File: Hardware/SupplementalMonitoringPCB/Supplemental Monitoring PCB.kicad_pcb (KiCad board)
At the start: 2 copper layers, 41.8 x 30.1 mm, 67 parts, among them J6 52465-2470, U10 INND-SS30RAB, U11 INND-SS30RAB, U2 SN74HCS595DYYR, U4 SN74HCS595DYYR, U5 TLV9002QDRQ1, U6 TLV9002QDRQ1, U7 INND-SS30RAB, U8 SN74HCS595DYYR

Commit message: schm actually done now whoops
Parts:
- U4: moved to B.Cu
- moved U4 100.5 mm to (211.9, 65.0), turned to 180 degrees
- moved U11 45.6 mm to (222.4, 44.2)
- moved U10 45.3 mm to (230.9, 44.2)
- moved U2 22.1 mm to (214.0, 44.4)
- moved C3 6.09 mm to (211.8, 60.2)
- moved R9 2.04 mm to (215.1, 60.0)
- moved R8 2.04 mm to (213.5, 70.1)
- moved R10 2.04 mm to (215.2, 70.0)
- moved R4 2.04 mm to (208.6, 70.2)
- moved R6 2.04 mm to (210.2, 70.2)
- moved R3 2.04 mm to (208.5, 60.1)
- moved R5 2.04 mm to (210.2, 60.0)
- moved R7 2.04 mm to (213.4, 60.0)
- moved U7 2.04 mm to (211.9, 65.0)

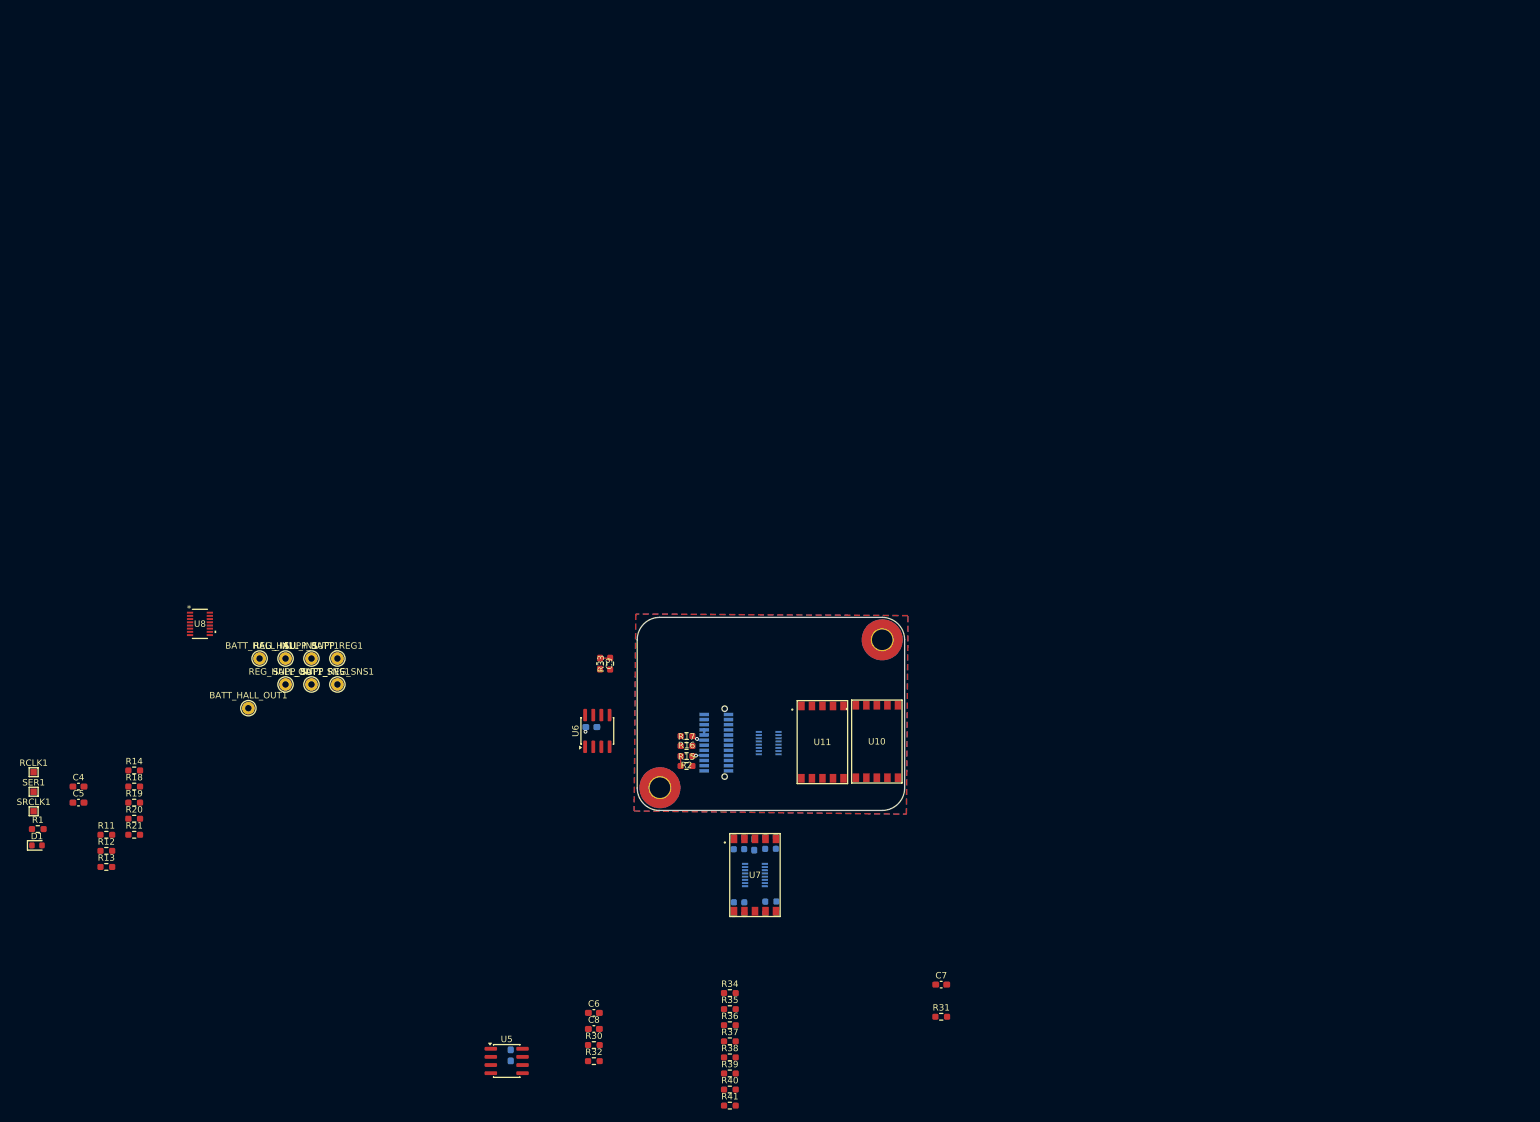
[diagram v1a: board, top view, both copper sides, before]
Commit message: seven segment routing
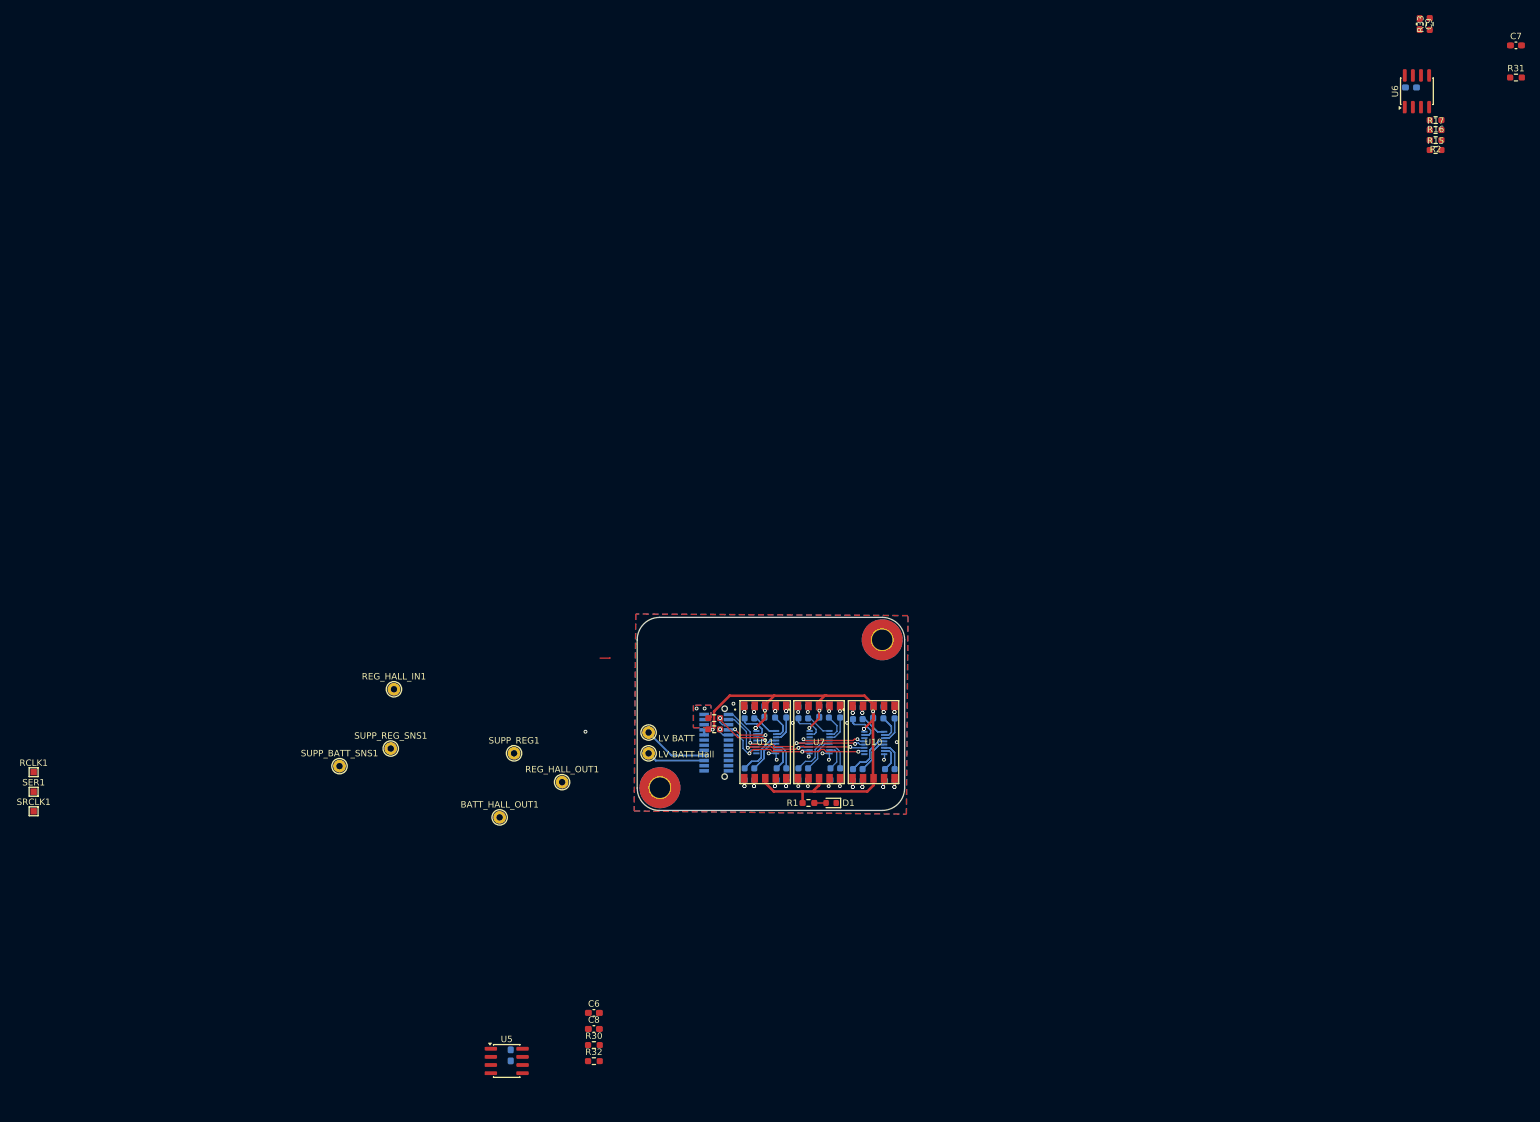
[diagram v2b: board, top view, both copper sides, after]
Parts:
- added R22: 1k, Resistor_SMD:R_0603_1608Metric_Pad0.98x0.95mm_HandSolder, F.Cu at (205.5, 42.2)
- added R23: 1k, Resistor_SMD:R_0603_1608Metric_Pad0.98x0.95mm_HandSolder, F.Cu at (205.5, 40.5)
- C4, C5, R11, R12, R13, R14, R18, R19, R20, R21, R34, R35, R36, R37, R38, R39, R40, R41, U8: moved to B.Cu
- moved C7 171.9 mm to (330.7, -64.5)
- moved R31 171.9 mm to (330.7, -59.5)
- moved C2 162.3 mm to (314.3, -58.0)
- moved C9 162.3 mm to (315.6, -67.9)
- moved R33 162.3 mm to (317.2, -67.9)
- moved U6 162.3 mm to (315.2, -57.4)
- moved R15 151.4 mm to (318.1, -48.2)
- moved R16 151.4 mm to (318.1, -52.9)
- moved R17 151.4 mm to (318.1, -51.3)
- moved R2 151.4 mm to (318.1, -49.7)
- moved C5 124.9 mm to (230.3, 39.6), turned to -90 degrees
- moved D1 124.2 mm to (223.8, 53.8), turned to 180 degrees
- moved R13 122.4 mm to (232.2, 49.4), turned to -90 degrees
- moved R1 120.4 mm to (220.2, 53.8)
- moved R21 120.2 mm to (233.7, 39.6), turned to -90 degrees
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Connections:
- J6 pad 10: unconnected-(J6-Pad10) -> /~{SRCLR}
- J6 pad 6: unconnected-(J6-Pad6) -> /~{OE}
- R10 pad 2: /Seven Segment/2b -> /Seven Segment/2d
- R12 pad 1: /Seven Segment/3d -> /Seven Segment/3f
- R13 pad 1: /Seven Segment/3c -> /Seven Segment/3h
- R14 pad 1: /Seven Segment/3h -> /Seven Segment/3g
- R18 pad 2: /Seven Segment/3g -> /Seven Segment/3a
- R19 pad 2: /Seven Segment/3f -> /Seven Segment/3b
- R20 pad 2: /Seven Segment/3a -> /Seven Segment/3c
- R21 pad 2: /Seven Segment/3b -> /Seven Segment/3d
- R34 pad 2: /Seven Segment/1g -> /Seven Segment/1a
- R36 pad 2: /Seven Segment/1f -> /Seven Segment/1b
- R37 pad 1: /Seven Segment/1d -> /Seven Segment/1f
- R38 pad 2: /Seven Segment/1a -> /Seven Segment/1c
- R39 pad 1: /Seven Segment/1c -> /Seven Segment/1h
- R4 pad 1: /Seven Segment/2d -> /Seven Segment/2f
- R40 pad 2: /Seven Segment/1b -> /Seven Segment/1d
- R41 pad 1: /Seven Segment/1h -> /Seven Segment/1g
- R5 pad 1: /Seven Segment/2c -> /Seven Segment/2h
- R6 pad 1: /Seven Segment/2h -> /Seven Segment/2g
- R7 pad 2: /Seven Segment/2g -> /Seven Segment/2a
- R8 pad 2: /Seven Segment/2f -> /Seven Segment/2b
- R9 pad 2: /Seven Segment/2a -> /Seven Segment/2c
- U2 pad 10: +3.3V -> /~{SRCLR}
- U2 pad 13: GND -> /~{OE}
- U4 pad 10: +3.3V -> /~{SRCLR}
- U4 pad 13: GND -> /~{OE}
- U8 pad 10: +3.3V -> /~{SRCLR}
- U8 pad 13: GND -> /~{OE}
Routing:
- net +3.3V: track 0.80 -> 95.2 mm, vias 1 -> 10
- net /~{SRCLR}: track 0.00 -> 29.1 mm, vias 0 -> 4
- net /SRCLK: track 0.00 -> 28.1 mm, vias 0 -> 3
- net /RCLK: track 0.00 -> 27.8 mm, vias 0 -> 3
- net /~{OE}: track 0.00 -> 23.2 mm, vias 0 -> 4
- net /Seven Segment/3e: track 0.00 -> 14.8 mm
- net /Seven Segment/1e: track 0.00 -> 14.8 mm
- net /Seven Segment/3f: track 0.00 -> 11.2 mm
- net /Seven Segment/1f: track 0.00 -> 11.2 mm
- net /Seven Segment/1a: track 0.00 -> 10.8 mm
- net /Seven Segment/3a: track 0.00 -> 10.8 mm
- net /Supp_Batt_I: track 0.00 -> 9.14 mm
- net /Seven Segment/1g: track 0.00 -> 9.12 mm
- net /Seven Segment/3g: track 0.00 -> 9.12 mm
- net /Seven Segment/1d: track 0.00 -> 8.50 mm
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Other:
- board text added: "LV BATT"
- board text added: "LV BATT Hall"

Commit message: routing mostly done
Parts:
- added GND1: TestPoint, TestPoint:TestPoint_THTPad_D2.0mm_Drill1.0mm, F.Cu at (203.0, 53.0)
- added TP_3V3: TestPoint, TestPoint:TestPoint_THTPad_D2.0mm_Drill1.0mm, F.Cu at (230.5, 52.5)
- C1: moved to F.Cu
- R10, R11, R12, R13, R14, R18, R19, R20, R21, R3, R34, R35, R36, R37, R38, R39, R4, R40, R41, R5, R6, R7, R8, R9: value 560 -> 470
- R15, R16, R17, R2: moved to B.Cu
- moved C7 163.6 mm to (198.0, 31.2), turned to -90 degrees
- moved R31 158.3 mm to (199.2, 28.8), turned to 180 degrees
- moved R33 149.3 mm to (207.2, 33.1)
- moved R15 145.8 mm to (198.0, 34.5), turned to -90 degrees
- moved C9 145.8 mm to (207.2, 29.6), turned to 90 degrees
- moved R2 145.1 mm to (200.0, 34.5), turned to 90 degrees
- moved R16 144.8 mm to (203.0, 35.0), turned to -90 degrees
- moved U6 144.1 mm to (202.5, 32.4), turned to 0 degrees
- moved C2 142.7 mm to (203.1, 31.4), turned to -90 degrees
- moved R17 142.5 mm to (204.8, 35.0), turned to 90 degrees
- moved LOGO2 105.3 mm to (182.7, 32.8)
- moved RCLK1 88.4 mm to (186.6, 35.1)
- moved SER1 88.4 mm to (186.6, 38.2)
- moved SRCLK1 88.4 mm to (186.6, 41.2)
- moved C1 81.7 mm to (224.5, 29.1), turned to 0 degrees
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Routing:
- net +3.3V: track 95.2 -> 140.6 mm, vias 10 -> 12
- net /Supp_Reg_I: track 0.00 -> 40.3 mm, vias 0 -> 3
- net /Supp_Batt_Vsns: track 0.00 -> 36.2 mm
- net /Supp_Reg_Isns: track 0.00 -> 33.4 mm, vias 0 -> 1
- net /Supp_Batt_I: track 9.14 -> 39.0 mm, vias 0 -> 3
- net /SuppReg_Vin: track 0.00 -> 27.8 mm, vias 0 -> 2
- net /Supp_Batt_Isns: track 0.00 -> 26.3 mm, vias 0 -> 1
- net GND: track 5.33 -> 22.0 mm, vias 11 -> 29
- net Net-(U2-QH'): track 0.00 -> 12.6 mm, vias 0 -> 3
- net Net-(U4-QH'): track 0.56 -> 12.4 mm, vias 1 -> 3
- net /Supp_Batt_Vin: track 10.2 -> 19.5 mm, vias 0 -> 1
- net /Seven Segment/1e: track 14.8 -> 7.34 mm
- net /~{OE}: track 23.2 -> 30.1 mm
- net /VoltageSense/vin2_divided: track 0.00 -> 4.57 mm, vias 0 -> 1
- net /VoltageSense/vin1_divided: track 0.00 -> 4.53 mm, vias 0 -> 1
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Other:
- board text added: "3v3"
- board text added: "GND"
- board text added: "LV Batt Isns"
- board text added: "LV Batt Vsns"
- board text added: "Reg Vsns"
- board text added: "Supp Vicor"
- board text added: "Vicor Hall"
- board text added: "Vicor Hall Out"

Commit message: board done and in cart
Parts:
- removed LOGO2: Dr. Hallock, UTSVT_Logos:Hallock_Image_Tiny
- removed RCLK1, SER1, SRCLK1: Test Point, TestPoint:TestPoint_Pad_1.0x1.0mm
- added J1: Conn_01x04, Connector_PinHeader_2.54mm:PinHeader_1x04_P2.54mm_Vertical, F.Cu at (214.2, 53.1)
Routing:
- net /SuppReg_Vsns: track 6.04 -> 25.6 mm, vias 1 -> 3
- net /SER: track 7.77 -> 23.1 mm, vias 2 -> 3
- net /RCLK: track 27.7 -> 37.9 mm
- net /SRCLK: track 28.1 -> 36.7 mm
- net +3.3V: track 140.6 -> 132.2 mm, vias 12 -> 10
- net /Seven Segment/3e: track 14.8 -> 7.38 mm
- net /Seven Segment/3f: track 11.2 -> 5.62 mm
- net /Seven Segment/3a: track 10.8 -> 5.42 mm
- net /Seven Segment/1a: track 10.8 -> 5.42 mm
- net /Seven Segment/1g: track 9.12 -> 4.56 mm
- net /Seven Segment/3g: track 9.12 -> 4.56 mm
- net /Seven Segment/1d: track 8.50 -> 4.25 mm
- net /Seven Segment/3d: track 8.50 -> 4.25 mm
- net /Seven Segment/1h: track 8.40 -> 4.20 mm
- net /Seven Segment/3h: track 8.40 -> 4.20 mm
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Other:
- board text added: "Supplemental Monitoring PCB Rev C Febuary 2026 Abigail Parsons"
